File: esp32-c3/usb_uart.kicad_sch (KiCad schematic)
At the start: 19 parts, among them J2 USB_C_Receptacle_USB2.0_16P, U4 CP2102N-Axx-xQFN28, U5 AMS1117-3.3

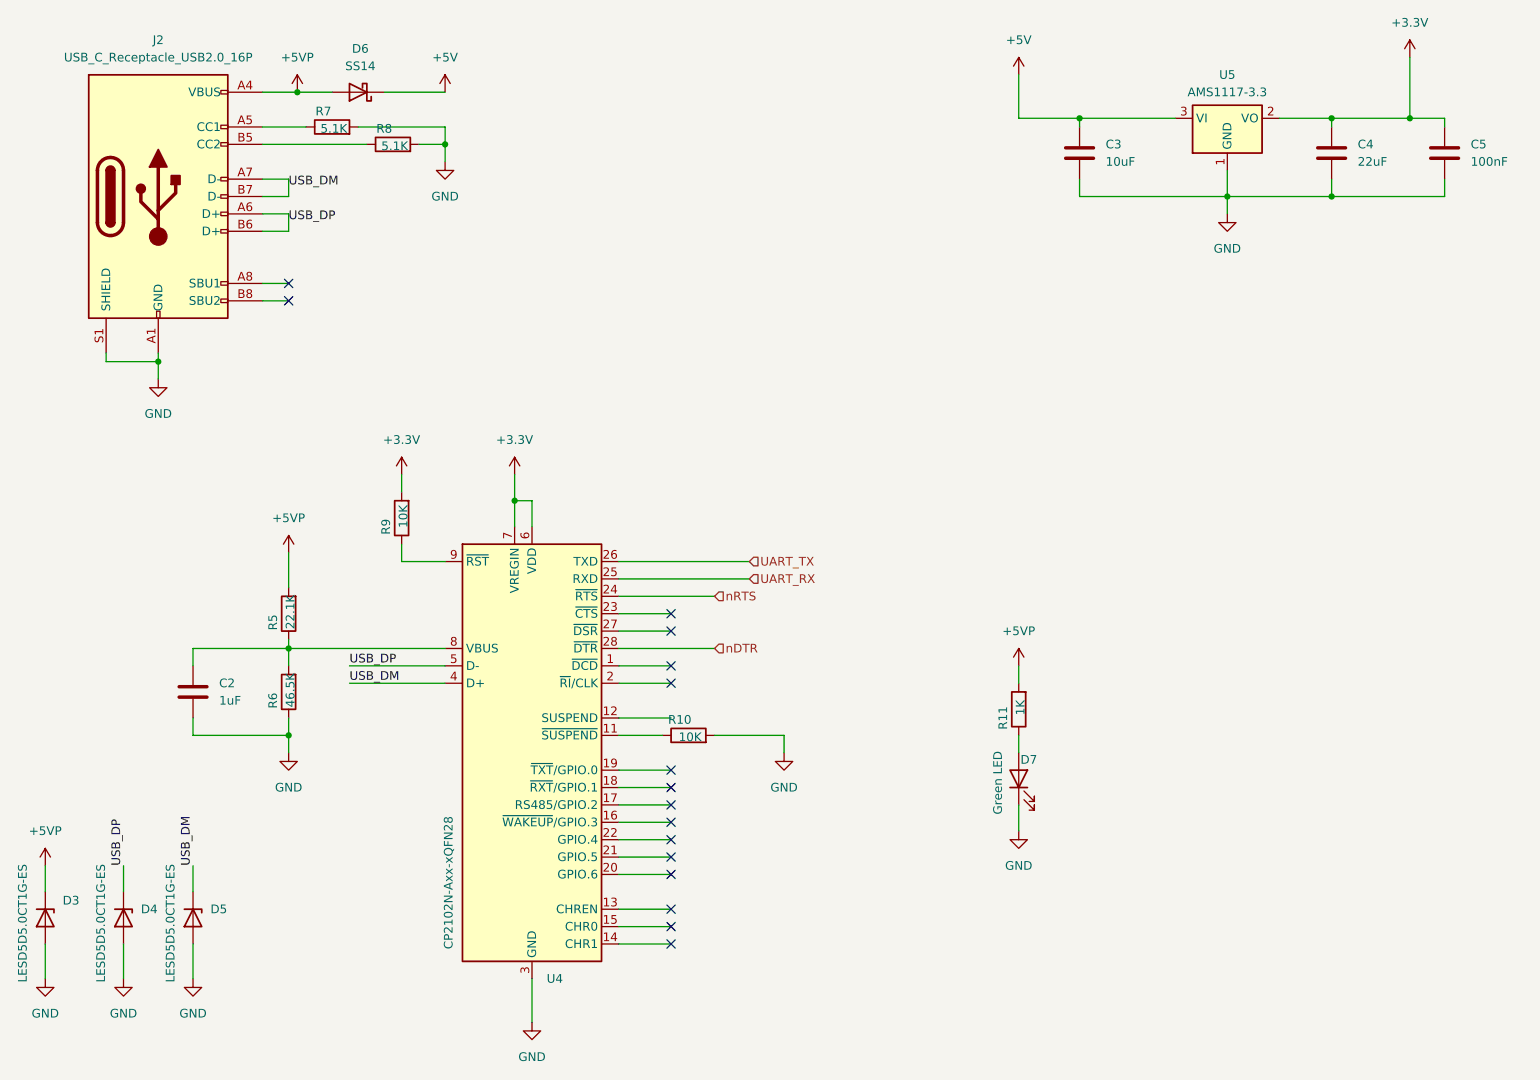
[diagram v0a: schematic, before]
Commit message: Fix Battery power and USB/UART connection, move vent around to accomodate enclosure
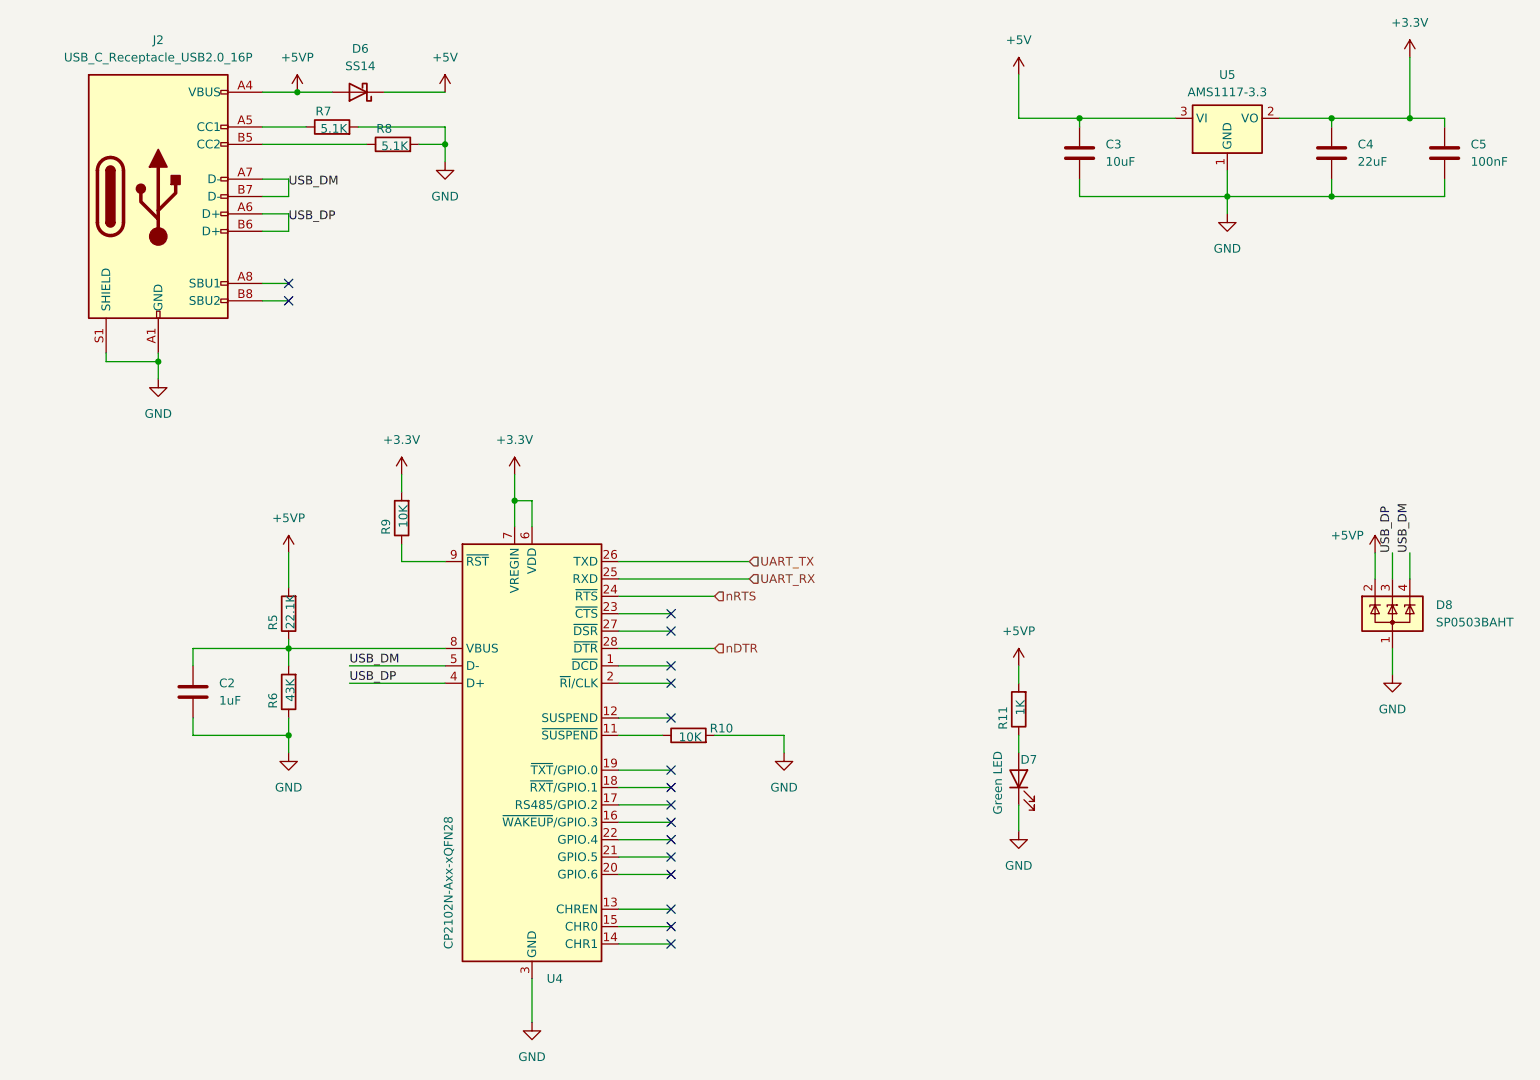
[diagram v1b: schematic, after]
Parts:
- removed D3, D4, D5: LESD5D5.0CT1G-ES, Diode_SMD:D_SOD-523, symbol Diode:ESD5Zxx
- added D8: SP0503BAHT, Package_TO_SOT_SMD:SOT-143, symbol Power_Protection:SP0503BAHT
- C2: LCSC (none) -> C52923
- C5: footprint Capacitor_SMD:C_0805_2012Metric -> Capacitor_SMD:C_0402_1005Metric
- J2: LCSC (none) -> C2894897
- R6: value 46.5K -> 43K
- U4: LCSC (none) -> C964632
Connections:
- net +5VP: now also D8.2 (K)
- net GND: now also D8.1 (A)
- net USB_DM: now also U4.5 (D-), D8.4 (K); no longer U4.4 (D+)
- net USB_DP: now also U4.4 (D+), D8.3 (K); no longer U4.5 (D-)
- no-connect marks 16 -> 17
